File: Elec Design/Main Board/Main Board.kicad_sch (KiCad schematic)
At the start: 23 parts, among them J1 302-S101, J2 LPC1768 Socket, J3 PJ-102A, J4 OSTTC020162, J5 OSTTC030162, J6 0022232041, U2 MCP2551-I-P, U3 NCP718xSN500, U4 NCP718xSN330

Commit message: converting to git structure
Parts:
- removed C2: 10uF, Capacitor_SMD:C_1206_3216Metric_Pad1.33x1.80mm_HandSolder, symbol Device:C
- removed D1: 1N5819HW-7-F, digikey-footprints:SOD-123, symbol dk_Diodes-Rectifiers-Single:1N5819HW-7-F
- removed J1: 302-S101, digikey-footprints:PinHeader_2x5_P2.54mm_Drill1.2mm, symbol dk_Rectangular-Connectors-Headers-Male-Pins:302-S101
- removed J2: LPC1768 Socket, Package_DIP:DIP-40_W22.86_Socket, symbol Connector_Generic:Conn_02x20_Counter_Clockwise
- removed U3: NCP718xSN500, Package_TO_SOT_SMD:SOT-23-5, symbol Regulator_Linear:NCP718xSN500
- added C1, C16, C17, C2: 18pF, Capacitor_SMD:C_0603_1608Metric, symbol Device:C
- added C10, C8: 22uF, Capacitor_SMD:C_0603_1608Metric, symbol Device:C
- added C12, C15, C7: 1uF, Capacitor_SMD:C_0603_1608Metric, symbol Device:C
- added C18 (x2), C20, C22, C24: 100nF, Capacitor_SMD:C_0603_1608Metric, symbol Device:C
- added C19, C21, C23: 10nF, Capacitor_SMD:C_0603_1608Metric, symbol Device:C
- added C2, C3: 0.1uF, Capacitor_SMD:C_0603_1608Metric, symbol Device:C
- added C6: 6800pF, Capacitor_SMD:C_0603_1608Metric, symbol Device:C
- added D1: B340, Diode_SMD:D_SMA, symbol Diode:B340
- added D4, D5: LED Low current, LED_SMD:LED_0603_1608Metric, symbol Device:LED
- added J3: Conn_ARM_JTAG_SWD_10, 10 pin jtag:CONN_3220-10-0100-00_CNC, symbol Connector:Conn_ARM_JTAG_SWD_10
- added L1: 4.7uH, NR6028T4R7M:IND_NR6028T4R7M, symbol Device:L
- added R1 (x3), R2: 10k, Resistor_SMD:R_0603_1608Metric, symbol Device:R
- added R15, R16 (x2), R19 (x2): 50R, Resistor_SMD:R_0603_1608Metric, symbol Device:R
- added R18: 100k, Resistor_SMD:R_0603_1608Metric, symbol Device:R
- added R20: 100R, Resistor_SMD:R_0603_1608Metric, symbol Device:R
- added R20, R21: 750R, Resistor_SMD:R_0603_1608Metric, symbol Device:R
- added R3: 430k, Resistor_SMD:R_0603_1608Metric, symbol Device:R
- added R4: 82k, Resistor_SMD:R_0603_1608Metric, symbol Device:R
- added SW1: SW_SPST, digikey-footprints:Switch_Tactile_SMD_6x6mm_PTS645, symbol Switch:SW_MEC_5E
- added U1: BD9E302EFJ-E2, HTSOP-J8_ROM, symbol BD9E302EFJ-E2:BD9E302EFJ-E2
- added U2: ESP32-C3-MINI-1, Espressif:ESP32-C3-MINI-1, symbol Espressif:ESP32-C3-MINI-1
- added U5: LPC1768FBD100, Package_QFP:LQFP-100_14x14mm_P0.5mm, symbol MCU_NXP_LPC:LPC1768FBD100
- added Y1: 12MHz/10pF, Crystal:Crystal_SMD_Abracon_ABM3B-4Pin_5.0x3.2mm, symbol Device:Crystal
- added Y2: 32.768kHz/9pF, Crystal:Crystal_SMD_3215-2Pin_3.2x1.5mm, symbol Device:Crystal
- C1, C4: footprint Capacitor_SMD:C_1206_3216Metric_Pad1.33x1.80mm_HandSolder -> Capacitor_SMD:C_0603_1608Metric; JLC? (none) -> N; MPN (none) -> C0603C104K5RECAUTO; Rated V 25V -> 50V
- C5: value 100nF -> 0.1uF; footprint Capacitor_SMD:C_1206_3216Metric_Pad1.33x1.80mm_HandSolder -> Capacitor_SMD:C_0603_1608Metric; JLC? (none) -> Y; MPN (none) -> CL10B104KB8NNWC; Rated V 25V -> 50V
- C9: renamed from C3; footprint Capacitor_SMD:C_0805_2012Metric_Pad1.18x1.45mm_HandSolder -> Capacitor_SMD:C_0603_1608Metric; DK_Detail_Page https://www.digikey.ca/en/products/detail/kyocera-avx/08055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 -> (none); JLC? (none) -> Y; MPN (none) -> C0603C102K4RECAUTO; Rated V 50V -> 16V
- D2, D3: JLC? (none) -> Y; MPN (none) -> XZCM2CRK53WA-8VF
- J1: renamed from J3; JLC? (none) -> N
- J2: renamed from J5; value OSTTC030162 -> ~; footprint digikey-footprints:Term_Block_1x3_P5mm -> 1x3 terminal block:CONN_282834-3_TYC; Category Connectors, Interconnects -> (none); DK_Datasheet_Link http://www.on-shore.com/wp-content/uploads/OSTTCXX0162.pdf -> (none); DK_Detail_Page /product-detail/en/on-shore-technology-inc/OSTTC030162/ED26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 -> (none); Digi-Key_PN ED2601-ND -> (none); Family Terminal Blocks - Wire to Board -> (none); JLC? (none) -> N; MPN OSTTC030162 -> 282834-3; Manufacturer On Shore Technology Inc. -> (none); Status Active -> (none)
- J4: renamed from J6; footprint digikey-footprints:PinHeader_1x4_P2.54mm_Drill1.02mm -> Connector_PinHeader_2.54mm:PinHeader_1x04_P2.54mm_Vertical; DK_Detail_Page /product-detail/en/molex/0022232041/WM4202-ND/26671 -> (none); JLC? (none) -> Y; MPN 0022232041 -> PPTC041LFBN
- J5: renamed from J4; value OSTTC020162 -> ~; footprint digikey-footprints:Term_Block_1x2_P5mm -> 1x2 terminal block:CONN2_282834-2_TEC; Category Connectors, Interconnects -> (none); DK_Datasheet_Link http://www.on-shore.com/wp-content/uploads/OSTTCXX0162.pdf -> (none); DK_Detail_Page /product-detail/en/on-shore-technology-inc/OSTTC020162/ED26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 -> (none); Digi-Key_PN ED2600-ND -> A98333-ND; Family Terminal Blocks - Wire to Board -> (none); JLC? (none) -> N; MPN OSTTC020162 -> 282834-2; Manufacturer On Shore Technology Inc. -> (none); Status Active -> (none)
- R14: renamed from R3; footprint Resistor_SMD:R_1206_3216Metric_Pad1.30x1.75mm_HandSolder -> Resistor_SMD:R_0603_1608Metric; JLC? (none) -> Y
- R17: renamed from R1; footprint Resistor_SMD:R_1206_3216Metric_Pad1.30x1.75mm_HandSolder -> Resistor_SMD:R_0603_1608Metric; DK_Detail_Page (none) -> https://www.digikey.ca/en/products/detail/stackpole-electro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; JLC? (none) -> Y; MPN (none) -> RMCF0201FT10K0
- R19: renamed from R2; footprint Resistor_SMD:R_1206_3216Metric_Pad1.30x1.75mm_HandSolder -> Resistor_SMD:R_0603_1608Metric; JLC? (none) -> Y
- R5: footprint Resistor_SMD:R_0805_2012Metric_Pad1.20x1.40mm_HandSolder -> Resistor_SMD:R_0603_1608Metric; DK_Detail_Page https://www.digikey.ca/en/products/detail/yageo/RC0805FR-07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 -> (none); JLC? (none) -> Y
- R8: renamed from R4; footprint Resistor_SMD:R_0805_2012Metric_Pad1.20x1.40mm_HandSolder -> Resistor_SMD:R_0603_1608Metric; DK_Detail_Page https://www.digikey.ca/en/products/detail/yageo/RC0805FR-07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 -> (none); JLC? (none) -> Y
- S1: footprint SW_L102021ML04Q -> Switches:SW_L102021ML04Q; JLC? (none) -> Y
- U3: renamed from U2; JLC? (none) -> Y
- U4: JLC? (none) -> N
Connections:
- net +3.3V: now also C15.1, C18.1, C19.1, C20.1, C21.1, C22.1, C23.1, C24.1, J3.1 (VTref), R1.1, R18.1, R2.2, U2.3 (3V3), U5.19 (VBAT), U5.28 (VDD(3V3)), U5.42 (VDD(REG)(3V3)), U5.54 (VDD(3V3)), U5.71 (VDD(3V3)), U5.84 (VDD(REG)(3V3)), U5.96 (VDD(3V3))
- net +5V: now also C10.1, C12.1, C8.1, L1.2
- net GND: now also C1.1, C10.2, C12.2, C15.2, C16.1, C17.1, C18.2, C18.2, C19.2, C2.2, C2.2, C20.2, C21.2, C22.2, C23.2, C24.2, C7.2, C8.2, D4.1 (K), D5.1 (K), J3.3 (GND), J3.5 (GND), J3.9 (GNDDetect), R1.2, R1.2, R4.2, SW1.3 (K), SW1.4 (A), U1.4 (AGND), U1.7 (PGND), U1.EPAD, U2.1 (GND), U2.11 (GND), U2.14 (GND), U2.2 (GND), U2.36 (GND), U2.37 (GND), U2.38 (GND), U2.39 (GND), U2.40 (GND), U2.41 (GND), U2.42 (GND), U2.43 (GND), U2.44 (GND), U2.45 (GND), U2.46 (GND), U2.47 (GND), U2.48 (GND), U2.49 (GND), U2.50 (GND), U2.51 (GND), U2.52 (GND), U2.53 (GND), U5.11 (VSSA), U5.15 (VREFN), U5.31 (VSS), U5.41 (VSS), U5.55 (VSS), U5.72 (VSS), U5.83 (VSS), U5.97 (VSS)
- net VBUS: now also S1.3, D1.1 (K); no longer C1.1
- net at U3.1 (TXD): now also U5.47 (P0[1])
- net at U3.4 (RXD): now also U5.46 (P0[0])
- new net: C1.1, C2.1, D1.2 (A), U1.2 (VIN), U1.3 (EN)
- new net: U2.16 (GPIO10), U5.24 (P0[28])
- new net: U2.18 (GPIO4/ADC1_CH4), U5.56 (P0[22])
- new net: U2.19 (GPIO5/ADC2_CH0), U5.9 (P0[23])
- new net: U2.20 (GPIO6), U5.8 (P0[24])
- new net: U2.21 (GPIO7), U5.7 (P0[25])
- new net: U2.22 (GPIO8), U5.6 (P0[26])
- new net: U2.23 (GPIO9), U5.25 (P0[27])
- new net: U2.30 (GPIO20/U0RXD), U5.62 (P0[15])
- new net: U2.31 (GPIO21/U0TXD), U5.63 (P0[16])
- new net: U2.5 (GPIO2/ADC1_CH2), U5.58 (P0[20])
- new net: U2.6 (GPIO3/ADC1_CH3), U5.57 (P0[21])
- new net: C7.1, R2.1, U2.8 (EN/CHIP_PU)
- new net: C2.1, U5.23 (XTAL2), Y1.1
- new net: J3.10 (~{RESET}), R19.1
- new net: J3.2 (SWDIO/TMS), R15.1
- new net: J3.4 (SWDCLK/TCK), R1.1, R19.1
- new net: J3.6 (SWO/TDO), R1.2, R16.1
- new net: J3.8 (NC/TDI), R16.1
- new net: C16.2, U5.16 (RTCX1), Y2.2
- new net: C3.1, U1.1 (BOOT)
- new net: C3.2, L1.1, R3.1, U1.8 (SW)
- new net: R21.1, U5.33 (P1[19])
- new net: D5.2 (A), R21.2
- new net: C6.2, R1.1
- new net: C17.2, U5.18 (RTCX2), Y2.1
- new net: C6.1, U1.6 (COMP)
- new net: R20.1, SW1.1, SW1.2
- new net: C1.2, U5.22 (XTAL1), Y1.2
- new net: R3.2, R4.1, U1.5 (FB)
- new net: D4.2 (A), R20.2
- new net: R20.1, U5.32 (P1[18])
- new net RESET: C18.1, R18.2, R19.2, R20.2, U5.17 (~{RESET})
- new net TCK: R19.2, U5.5 (TCK/SWDCLK)
- new net TDI: R16.2, U5.2 (TDI)
- new net TDO: R16.2, U5.1 (TDO/SWO)
- new net TMS: R15.2, U5.3 (TMS/SWDIO)
- new net nTRST: U5.4 (~{TRST})
- no-connect marks 42 -> 65
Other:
- note added: "Reset SW"
- note added: "Wakeup P0.20"
- note removed: "RXD"
- note removed: "TXD"
- moved on the sheet: C1, C9, D2, D3, J1, J2, J4, J5, R14, R17, R19, R5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

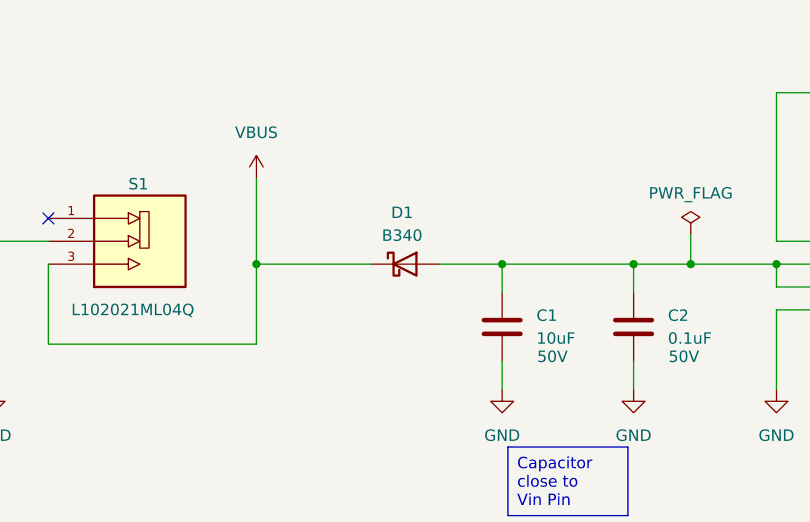
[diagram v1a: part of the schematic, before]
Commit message: corrected barrier diode direction on both boards
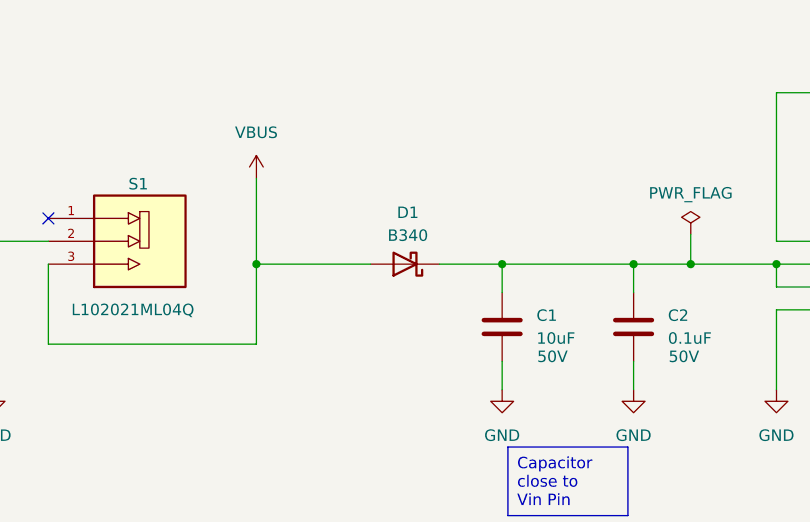
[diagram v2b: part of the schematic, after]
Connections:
- net VBUS: now also D1.2 (A); no longer D1.1 (K)
- net at C1.1, C2.1, U1.2 (VIN)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: now also D1.1 (K); no longer D1.2 (A)
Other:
- moved on the sheet: D1
